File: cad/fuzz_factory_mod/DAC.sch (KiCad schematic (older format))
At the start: 32 parts

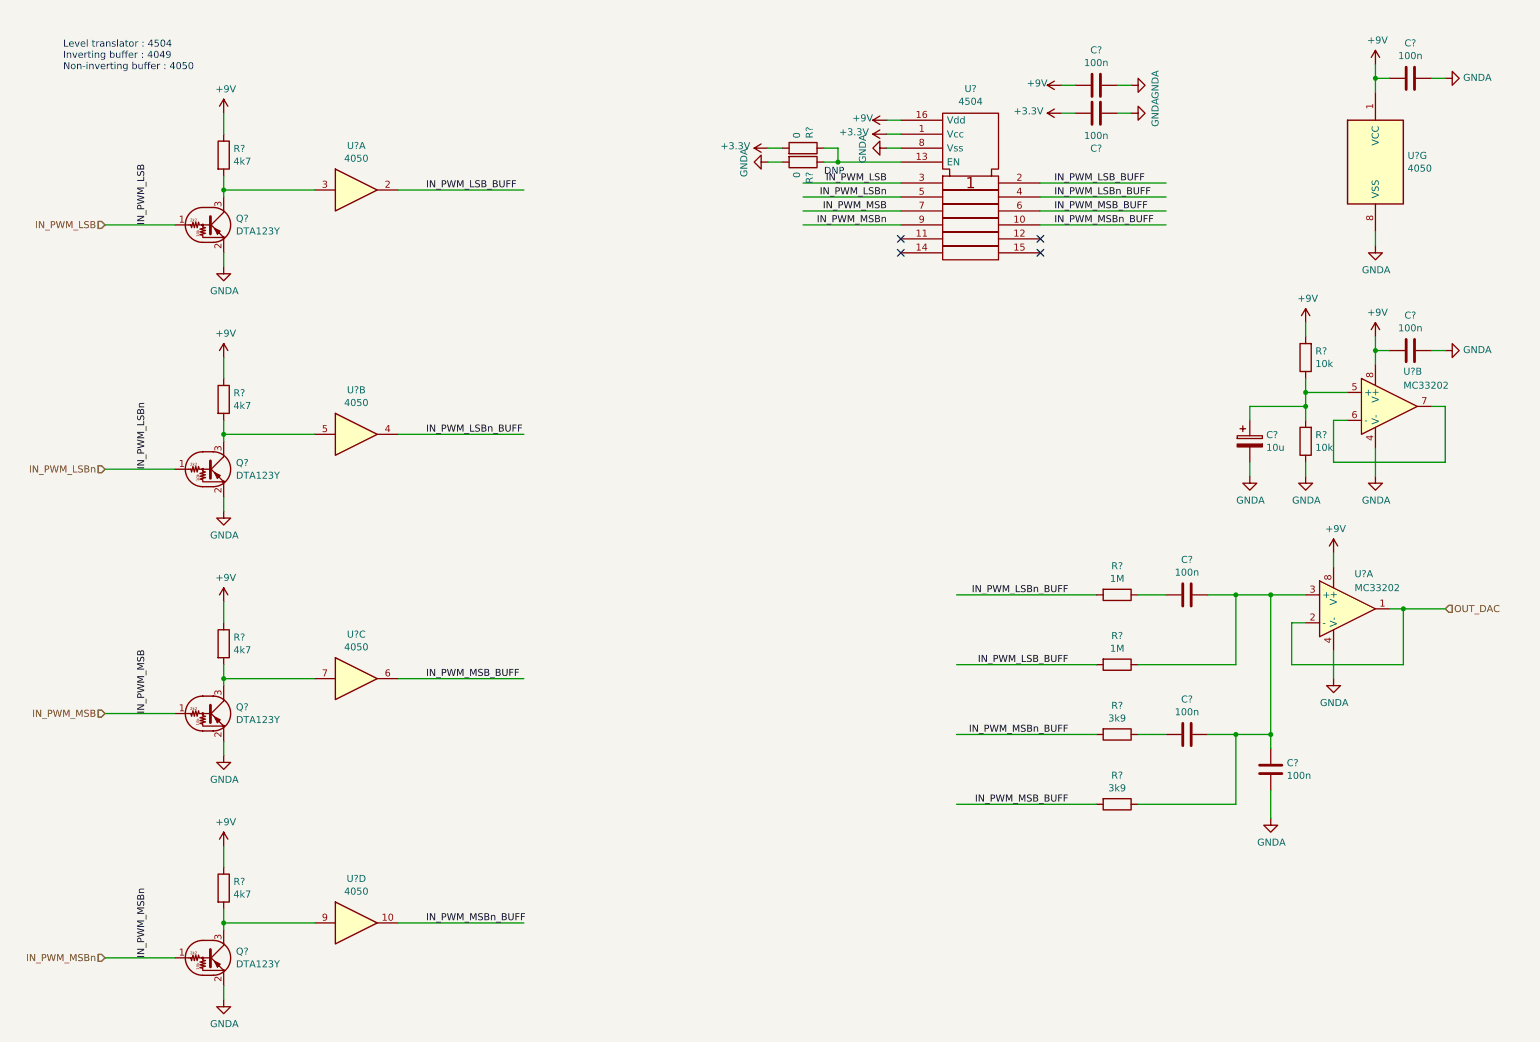
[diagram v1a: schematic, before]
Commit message: Continued schematic.
Modified fuuz_factory circuit : use of matched transistor pairs.
Added USB interface, through FT230X and direct to MCU.
Associated footprints, except for XTAL and trimmers.
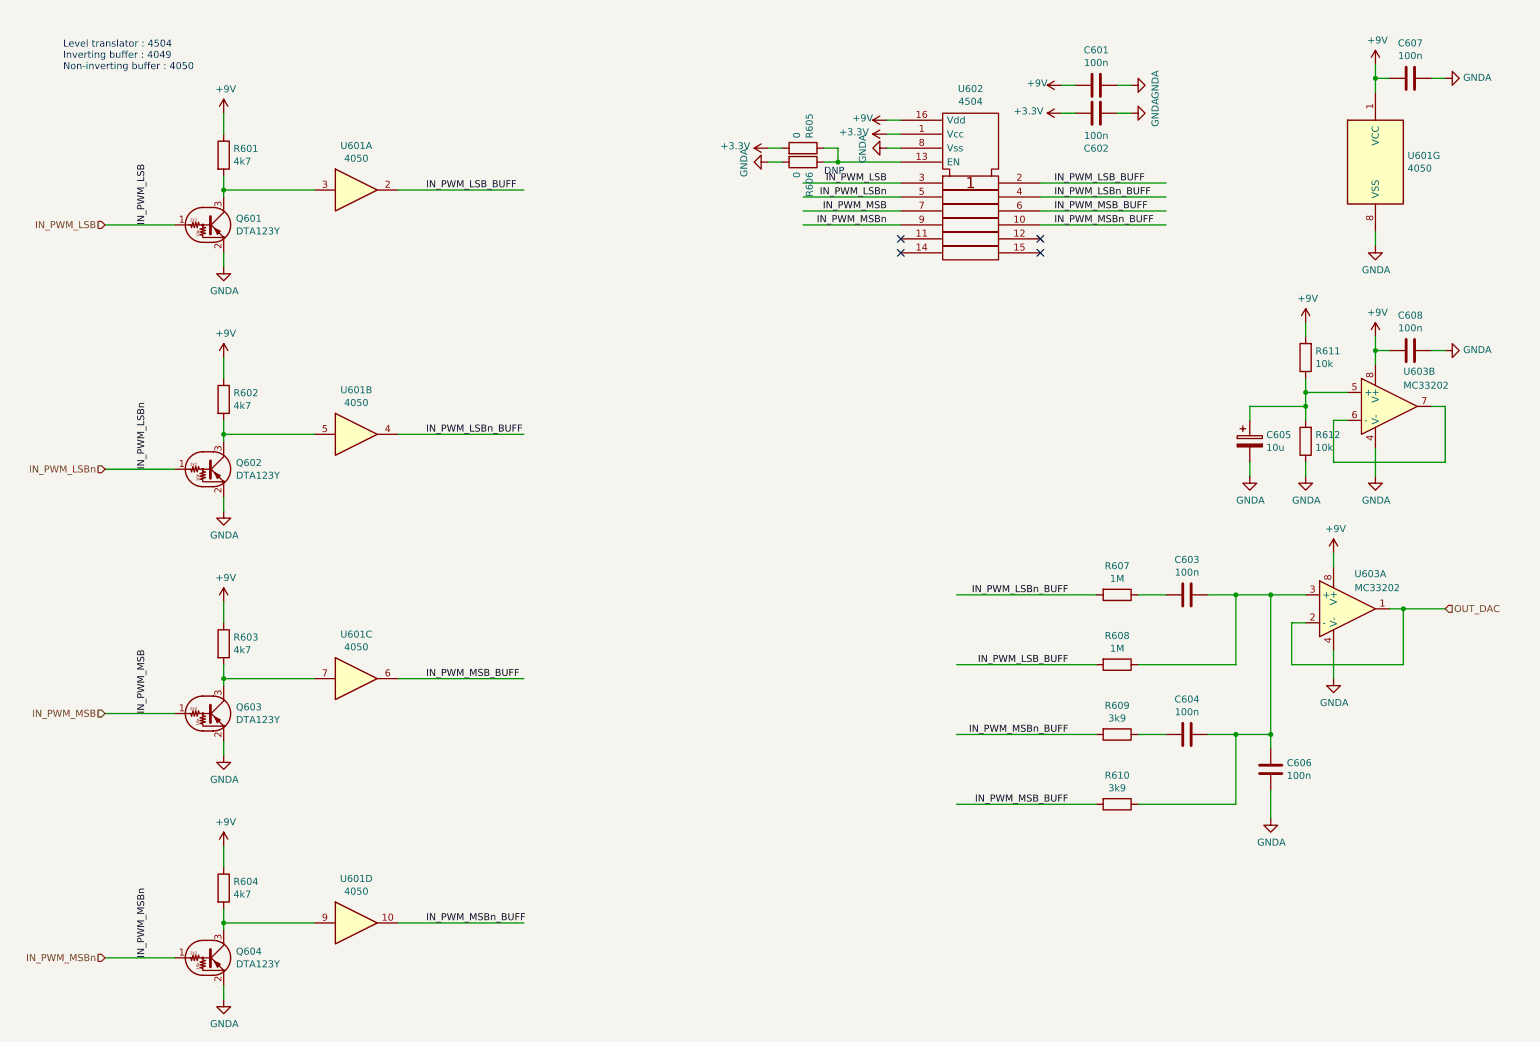
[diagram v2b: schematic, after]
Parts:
- C601, C602, C603, C604, C606, C607, C608: renamed from C?; footprint (none) -> Capacitors_SMD:C_0603
- C605: renamed from C?; footprint (none) -> Capacitors_SMD:CP_Elec_6.3x4.5
- Q601, Q602, Q603, Q604: renamed from Q?; footprint (none) -> TO_SOT_Packages_SMD:SOT-23
- R601, R602, R603, R604, R605, R606, R607, R608, R609, R610, R611, R612: renamed from R?; footprint (none) -> Resistors_SMD:R_0603
- U601, U602: renamed from U?; footprint (none) -> Housings_SOIC:SOIC-16_3.9x9.9mm_Pitch1.27mm
- U603: renamed from U?; footprint (none) -> Housings_SOIC:SOIC-8_3.9x4.9mm_Pitch1.27mm

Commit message: Continued schematic.
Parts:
- added C609: 100n, Capacitors_SMD:C_0603, symbol Device:C
- added R613, R614, R615, R616: 0, Resistors_SMD:R_0603, symbol Device:R
- added U604: 4049, Housings_SOIC:SOIC-16_3.9x9.9mm_Pitch1.27mm, symbol 4xxx:4049
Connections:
- wire segments 99 -> 128
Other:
- moved on the sheet: C1607, C1608, R1621, R1622, U1603

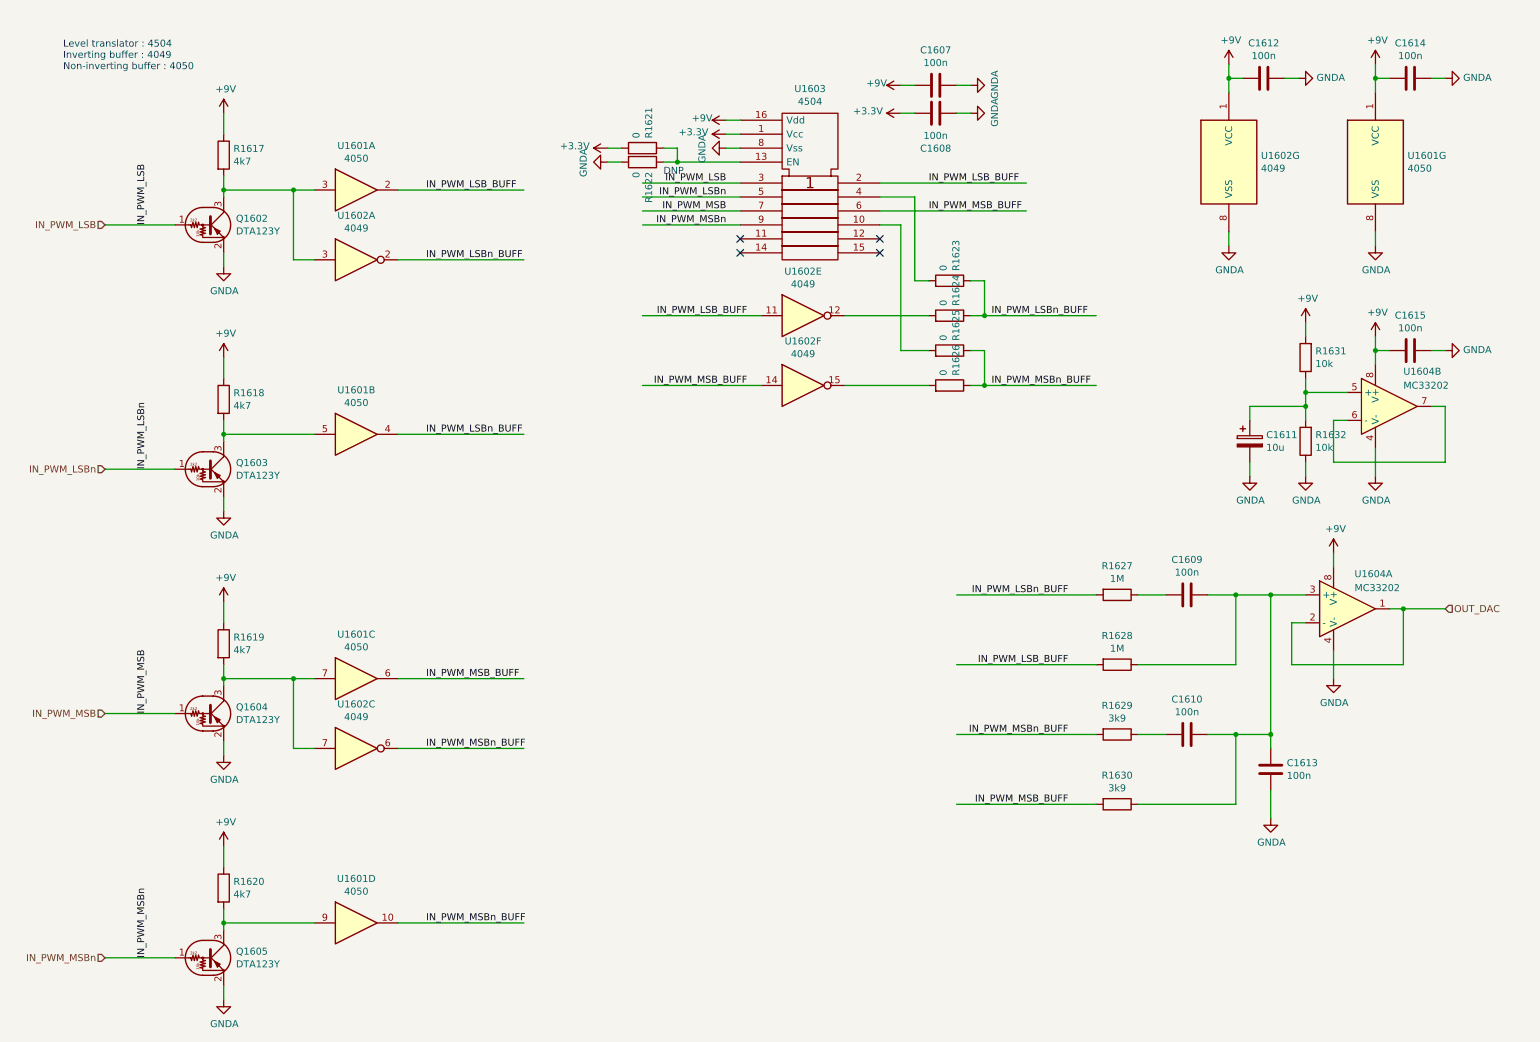
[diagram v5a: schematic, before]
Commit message: Changes architecture.
Corrections on schematic.
Continued Layout placement.
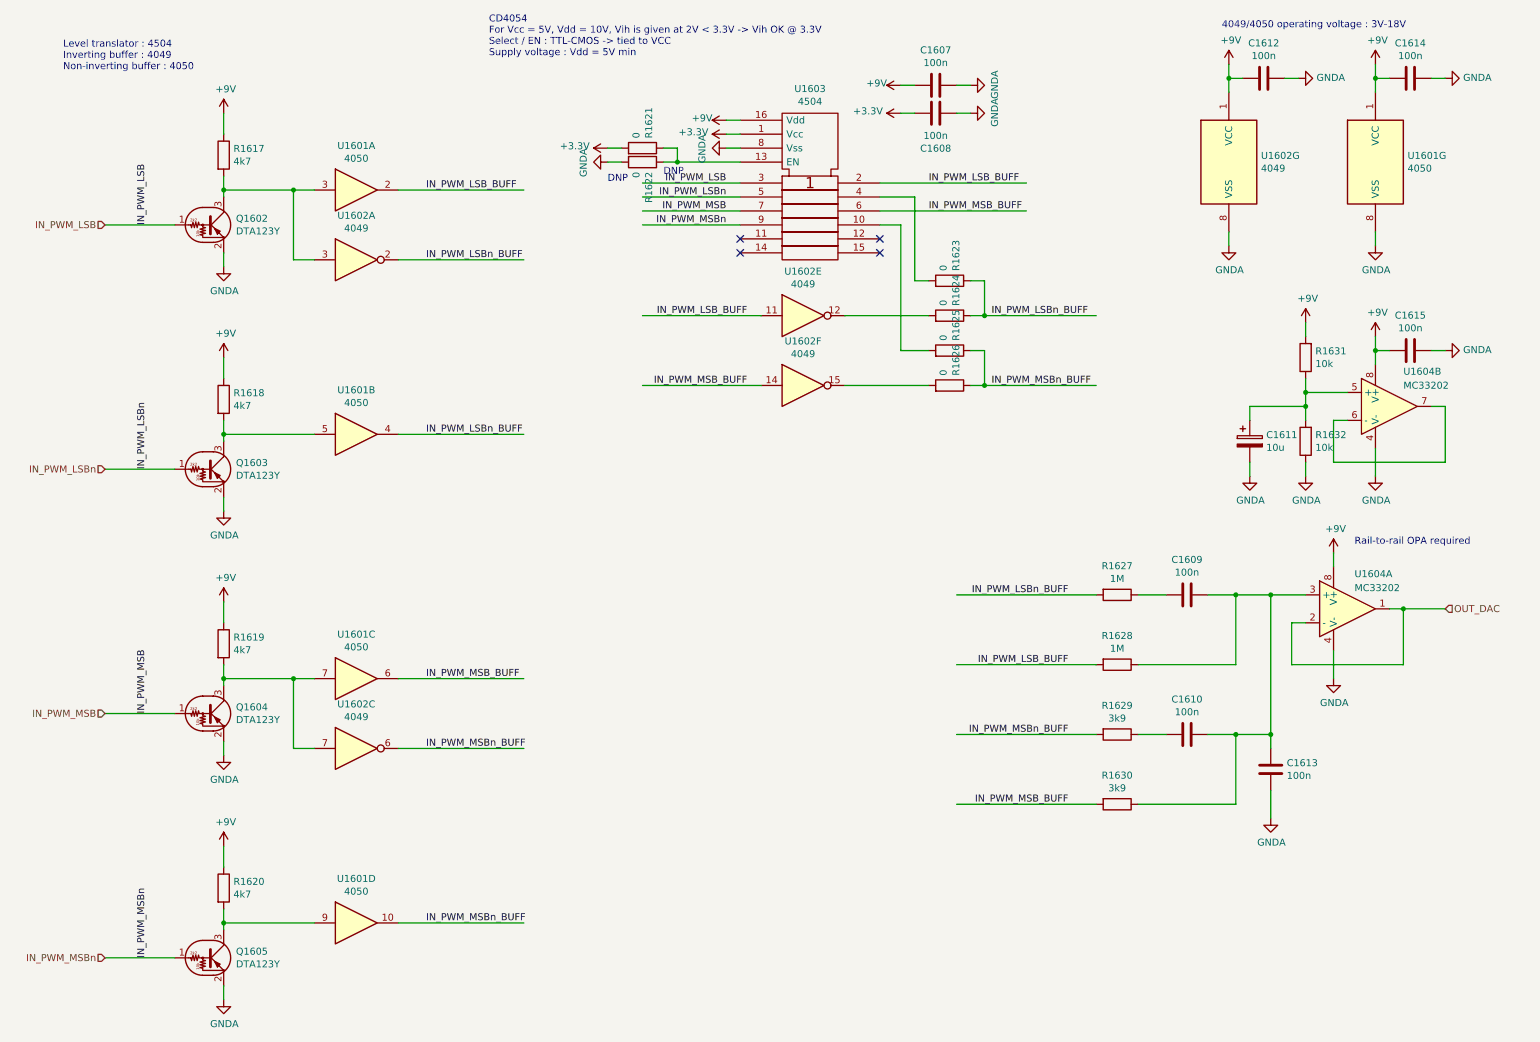
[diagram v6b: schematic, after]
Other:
- note added: "4049/4050 operating voltage : 3V-18V"
- note added: "CD4054\nFor Vcc = 5V, Vdd = 10V, Vih is given at 2V < 3.3V -> Vih OK @ 3.3V\nSelect / EN : TTL-CMOS -> tied to VCC\nSupply voltage : Vdd = 5V min"
- note added: "Rail-to-rail OPA required"
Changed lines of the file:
@@
 $Descr A4 11693 8268
 encoding utf-8
-Sheet 14 30
+Sheet 17 22
 Title ""
 Date ""
@@
 Wire Wire Line
 	6950 2400 6950 1800
+Text Notes 3900 800  0    50   ~ 0
+CD4054\nFor Vcc = 5V, Vdd = 10V, Vih is given at 2V < 3.3V -> Vih OK @ 3.3V\nSelect / EN : TTL-CMOS -> tied to VCC\nSupply voltage : Vdd = 5V min
+Text Notes 9150 600  0    50   ~ 0
+4049/4050 operating voltage : 3V-18V
+Text Notes 10100 4300 0    50   ~ 0
+Rail-to-rail OPA required
+Text Notes 4750 1700 0    50   ~ 0
+DNP
 $EndSCHEMATC

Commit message: Updated trimmers footprint.
Continued layout.
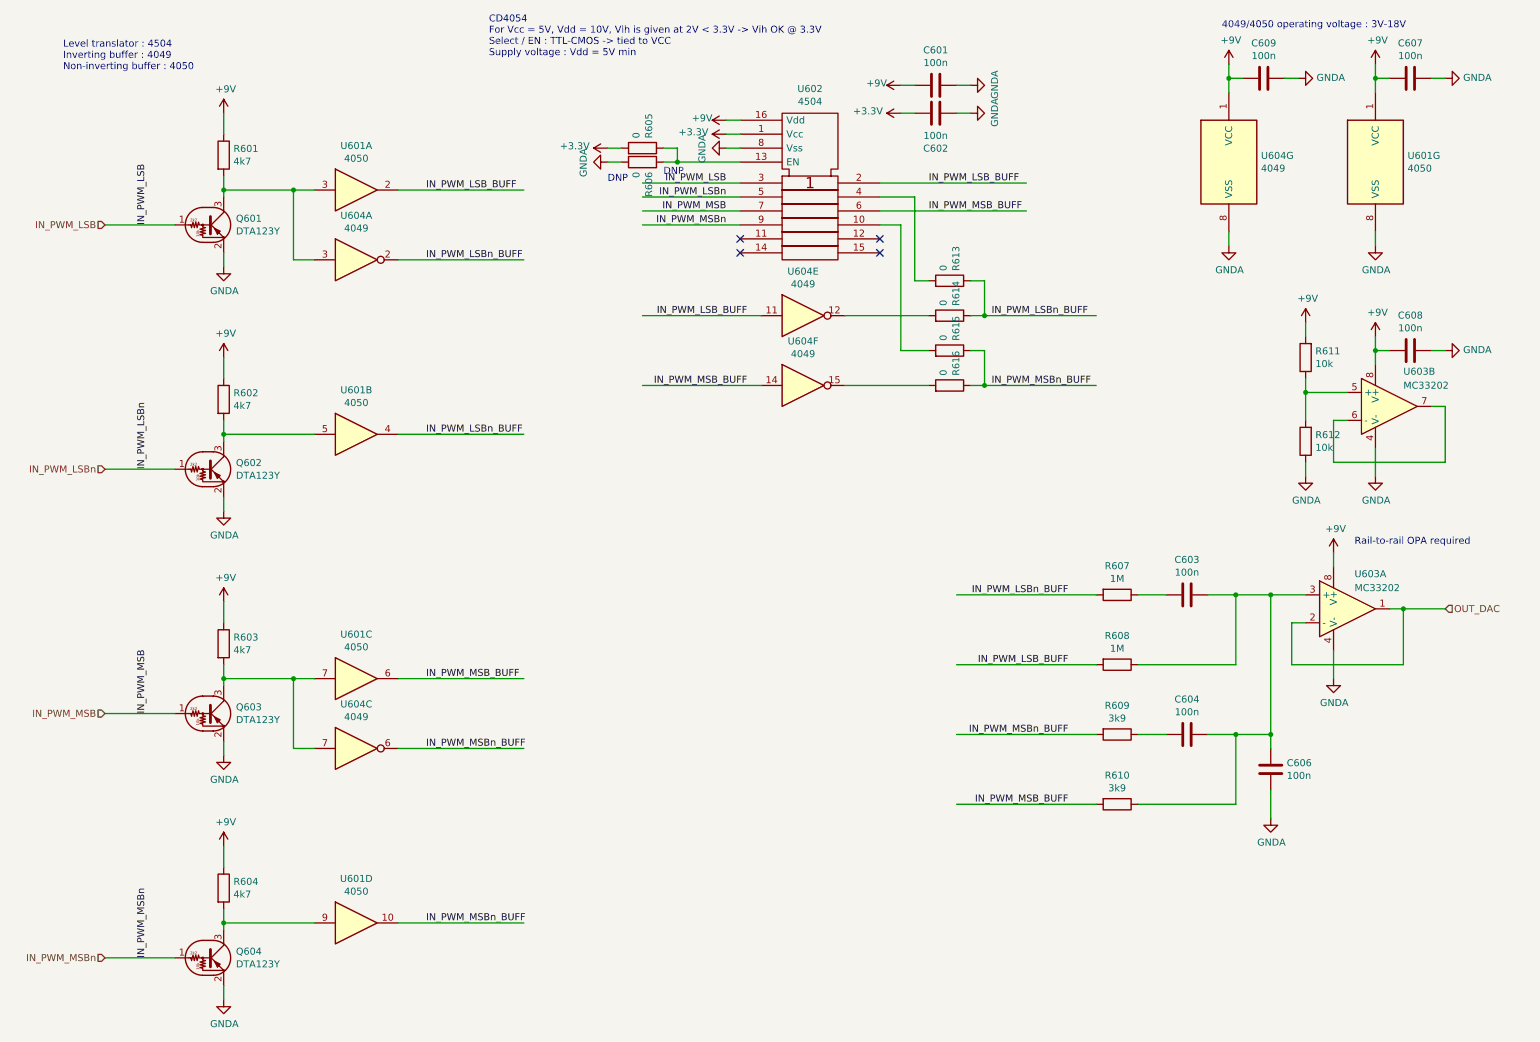
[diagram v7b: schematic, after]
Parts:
- removed C605: 10u, Capacitors_SMD:CP_Elec_6.3x4.5, symbol Device:CP
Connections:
- wire segments 128 -> 124
